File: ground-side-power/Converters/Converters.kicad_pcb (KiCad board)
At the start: 2 copper layers, 30 parts, among them J10 Conn_01x03_Female, J11 Conn_01x03_Female, J12 Conn_01x04_Female, J13 DAQ Voltage Sensing, J14 DAQ Current Sensing, J26 Conn_01x02_Female, U3 K7805-3AR3, U4 INA180, U5 INA180, U6 URB2424LD-20WR3

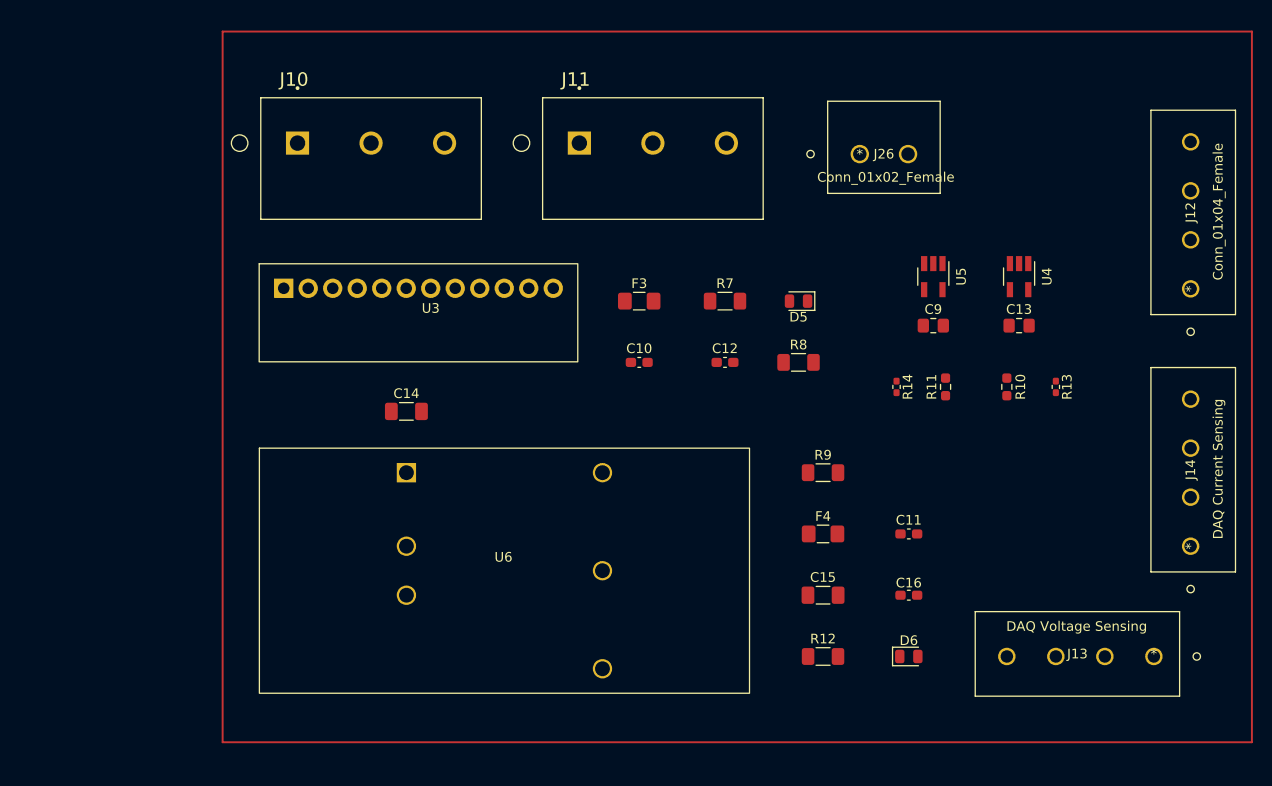
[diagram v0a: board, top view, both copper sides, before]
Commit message: Added Fan Headers + Thermistor
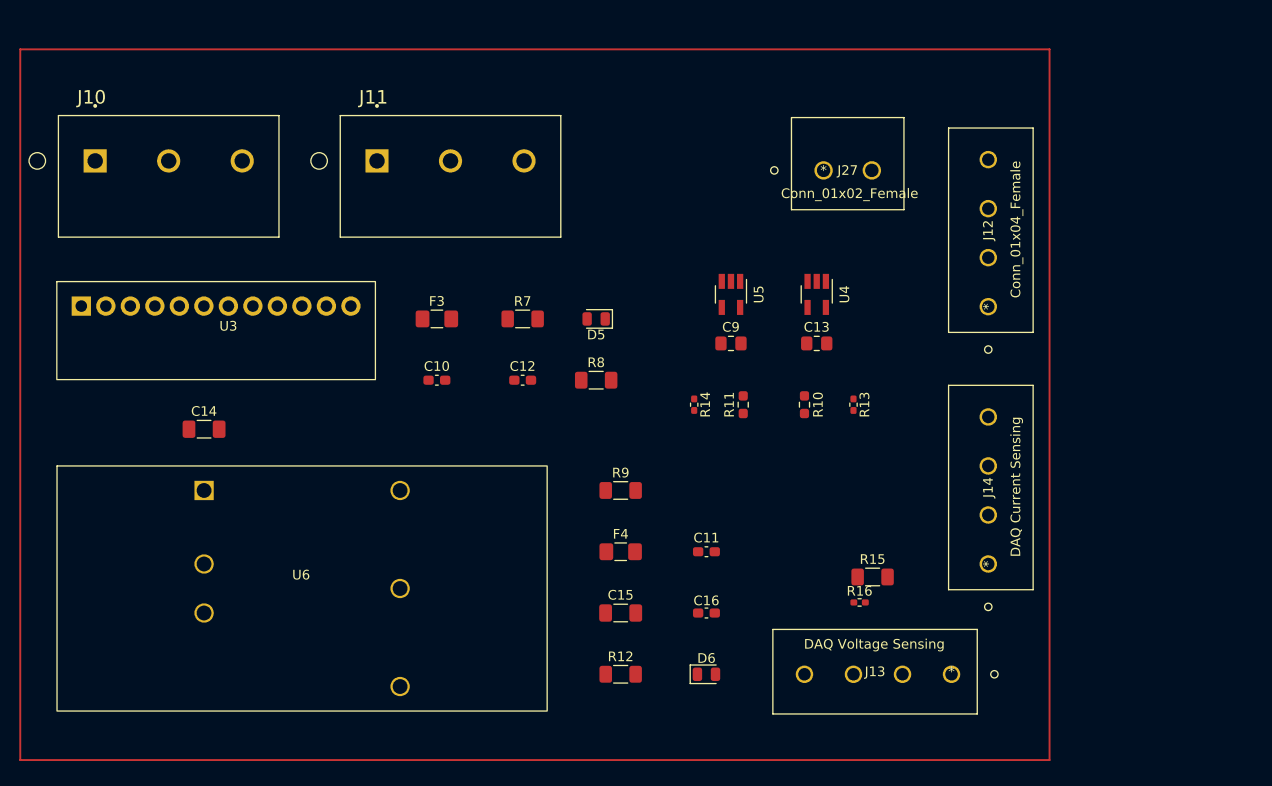
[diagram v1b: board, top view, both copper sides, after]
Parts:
- removed J26: Conn_01x02_Female, GSP:OSTTA020161
- added J27: Conn_01x02_Female, GSP:OSTTA020161, F.Cu at (158.8, 80.4)
- added R15: B57621C5103K062, Resistor_SMD:R_1206_3216Metric_Pad1.30x1.75mm_HandSolder, F.Cu at (163.9, 122.6)
- added R16: 10K, Resistor_SMD:R_0402_1005Metric_Pad0.72x0.64mm_HandSolder, F.Cu at (162.5, 125.2)
- moved C12 21.1 mm to (127.6, 102.2)
- moved C15 21.1 mm to (137.8, 126.3)
- moved C9 21.1 mm to (149.2, 98.4)
- moved D5 21.1 mm to (135.2, 95.8)
- moved F4 21.1 mm to (137.8, 120.0)
- moved J12 21.1 mm to (175.9, 94.6)
- moved J14 21.1 mm to (175.9, 121.2)
- moved R10 21.1 mm to (156.8, 104.7)
- moved R12 21.1 mm to (137.8, 132.7)
- moved R13 21.1 mm to (161.9, 104.7)
- moved R14 21.1 mm to (145.4, 104.7)
- moved R7 21.1 mm to (127.6, 95.8)
- moved R8 21.1 mm to (135.2, 102.2)
- moved R9 21.1 mm to (137.8, 113.6)
- moved U3 21.1 mm to (95.9, 97.1)
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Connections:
- C10 pad 1: (no net) -> Net-(C10-Pad1)
- C10 pad 2: (no net) -> GND
- C11 pad 1: (no net) -> +BATT
- C11 pad 2: (no net) -> GND
- C12 pad 1: (no net) -> +5V
- C12 pad 2: (no net) -> GND
- C13 pad 1: (no net) -> GND
- C13 pad 2: (no net) -> +5V
- C14 pad 1: (no net) -> +BATT
- C14 pad 2: (no net) -> GND
- C15 pad 1: (no net) -> Net-(C15-Pad1)
- C15 pad 2: (no net) -> GND
- C16 pad 1: (no net) -> +24V
- C16 pad 2: (no net) -> GND
- C9 pad 1: (no net) -> GND
- C9 pad 2: (no net) -> +5V
- D5 pad 1: (no net) -> Net-(D5-Pad1)
- D5 pad 2: (no net) -> +5V
- D6 pad 1: (no net) -> Net-(D6-Pad1)
- D6 pad 2: (no net) -> +24V
- F3 pad 1: (no net) -> Net-(C10-Pad1)
- F3 pad 2: (no net) -> /5V_Sense+
- F4 pad 1: (no net) -> Net-(C15-Pad1)
- F4 pad 2: (no net) -> /24V_Sense+
- J10 pad 1: (no net) -> +BATT
- J10 pad 2: (no net) -> /+12V
- J10 pad 3: (no net) -> GND
- J11 pad 1: (no net) -> /12V_OUT
- J11 pad 2: (no net) -> /TOTAL_OUT
- J11 pad 3: (no net) -> /12_VOLTAGE
- J12 pad 1: (no net) -> +5V
- J12 pad 2: (no net) -> /+12V
- J12 pad 3: (no net) -> +24V
- J12 pad 4: (no net) -> GND
- J13 pad 1: (no net) -> /Temp
- J13 pad 2: (no net) -> /5V_VOLTAGE
- J13 pad 3: (no net) -> /12_VOLTAGE
- J13 pad 4: (no net) -> /24V_VOLTAGE
- J14 pad 1: (no net) -> /TOTAL_OUT
- J14 pad 2: (no net) -> /5V_OUT
- J14 pad 3: (no net) -> /12V_OUT
- J14 pad 4: (no net) -> /24V_OUT
- R10 pad 1: (no net) -> +24V
- R10 pad 2: (no net) -> /24V_VOLTAGE
- R11 pad 1: (no net) -> +5V
- R11 pad 2: (no net) -> /5V_VOLTAGE
- R12 pad 1: (no net) -> GND
- R12 pad 2: (no net) -> Net-(D6-Pad1)
- R13 pad 1: (no net) -> /24V_VOLTAGE
- R13 pad 2: (no net) -> GND
- R14 pad 1: (no net) -> /5V_VOLTAGE
- R14 pad 2: (no net) -> GND
- R7 pad 1: (no net) -> /5V_Sense+
- R7 pad 2: (no net) -> +5V
- R8 pad 1: (no net) -> GND
- R8 pad 2: (no net) -> Net-(D5-Pad1)
- R9 pad 1: (no net) -> +24V
- R9 pad 2: (no net) -> /24V_Sense+
- U3 pad 1: (no net) -> unconnected-(U3-Pad1)
- U3 pad 10: (no net) -> Net-(C10-Pad1)
- U3 pad 11: (no net) -> Net-(C10-Pad1)
- U3 pad 12: (no net) -> unconnected-(U3-Pad12)
- U3 pad 2: (no net) -> +BATT
- U3 pad 3: (no net) -> +BATT
- U3 pad 4: (no net) -> +BATT
- U3 pad 5: (no net) -> GND
- U3 pad 6: (no net) -> GND
- U3 pad 7: (no net) -> GND
- U3 pad 8: (no net) -> GND
- U3 pad 9: (no net) -> Net-(C10-Pad1)
- U4 pad 1: (no net) -> /5V_OUT
- U4 pad 2: (no net) -> GND
- U4 pad 3: (no net) -> /5V_Sense+
- U4 pad 4: (no net) -> +5V
- U4 pad 5: (no net) -> +5V
- U5 pad 1: (no net) -> /24V_OUT
- U5 pad 2: (no net) -> GND
- U5 pad 3: (no net) -> /24V_Sense+
- U5 pad 4: (no net) -> +24V
- U5 pad 5: (no net) -> +5V
- U6 pad 1: (no net) -> unconnected-(U6-Pad1)
- U6 pad 2: (no net) -> GND
- U6 pad 3: (no net) -> +BATT
- U6 pad 4: (no net) -> Net-(C15-Pad1)
- U6 pad 5: (no net) -> GND
- U6 pad 6: (no net) -> unconnected-(U6-Pad6)

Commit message: PCB Layout First Draft
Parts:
- added ?: , clipboard:6b5716c7-8553-4764-af17-05841c85de2e, F.Cu at (152.4, 68.7)
- added ?: , clipboard:6b5716c7-8553-4764-af17-05841c85de2e, F.Cu at (152.1, 132.5)
- added ?: , clipboard:6b5716c7-8553-4764-af17-05841c85de2e, F.Cu at (81.2, 132.0)
- added ?: , clipboard:6b5716c7-8553-4764-af17-05841c85de2e, F.Cu at (81.3, 69.3)
- C11, C13, C14, C15, C9, F3, F4, R10, R11, R13, R14, R15, R16, R7, R9, U4, U5: moved to B.Cu
- moved J13 75.4 mm to (96.7, 134.2), turned to 0 degrees
- moved R16 69.9 mm to (92.7, 129.0), turned to 180 degrees
- moved R15 66.7 mm to (97.5, 129.0), turned to 180 degrees
- moved J14 59.1 mm to (118.3, 134.2), turned to 0 degrees
- moved R13 56.2 mm to (111.3, 129.0), turned to 180 degrees
- moved R11 49.9 mm to (106.9, 129.0), turned to 180 degrees
- moved R14 49.2 mm to (102.6, 129.0), turned to 180 degrees
- moved C11 48.9 mm to (105.4, 93.7), turned to 90 degrees
- moved R10 48.1 mm to (115.3, 129.0), turned to 180 degrees
- moved J10 46.2 mm to (129.5, 79.2), turned to 180 degrees
- moved U5 42.1 mm to (125.7, 128.3), turned to 0 degrees
- moved C13 41.1 mm to (131.1, 129.3), turned to 180 degrees
- moved U4 30.7 mm to (127.5, 90.9)
- moved J12 27.7 mm to (149.1, 101.4)
- moved R8 27.4 mm to (149.9, 79.0)
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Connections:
- J11 pad 1: /12V_OUT -> /12_VOLTAGE
- J11 pad 3: /12_VOLTAGE -> /12V_OUT
- J12 pad 1: +5V -> +24V
- J12 pad 2: /+12V -> GND
- J12 pad 3: +24V -> /+12V
- J12 pad 4: GND -> +5V
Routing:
- net +5V: track 0.00 -> 137.9 mm, vias 0 -> 3
- net /12V_OUT: track 0.00 -> 105.7 mm
- net /TOTAL_OUT: track 0.00 -> 96.9 mm
- net /12_VOLTAGE: track 0.00 -> 87.9 mm
- net +24V: track 0.00 -> 78.0 mm
- net /5V_OUT: track 0.00 -> 71.3 mm, vias 0 -> 2
- net /+12V: track 0.00 -> 32.1 mm
- net GND: track 0.00 -> 27.7 mm, vias 0 -> 6
- net Net-(C10-Pad1): track 0.00 -> 15.8 mm
- net /Temp: track 0.00 -> 12.1 mm
- net /24V_OUT: track 0.00 -> 11.5 mm
- net /24V_VOLTAGE: track 0.00 -> 11.4 mm
- net Net-(C15-Pad1): track 0.00 -> 10.9 mm
- net /5V_VOLTAGE: track 0.00 -> 10.6 mm
- net /24V_Sense+: track 0.00 -> 10.2 mm
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- added copper zone on B.Cu, net +BATT
- added copper zone on F.Cu, net GND
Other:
- board outline added: 81.8 x 73.7 mm
- board text added: "+12"
- board text added: "+12 Current"
- board text added: "+12 Voltage"
- board text added: "+24"
- board text added: "+5"
- board text added: "+BATT"
- board text added: "0"
- board text added: "Current"
- board text added: "Temp"
- board text added: "Total"
- board text added: "Total Current"
- board text added: "Voltage"

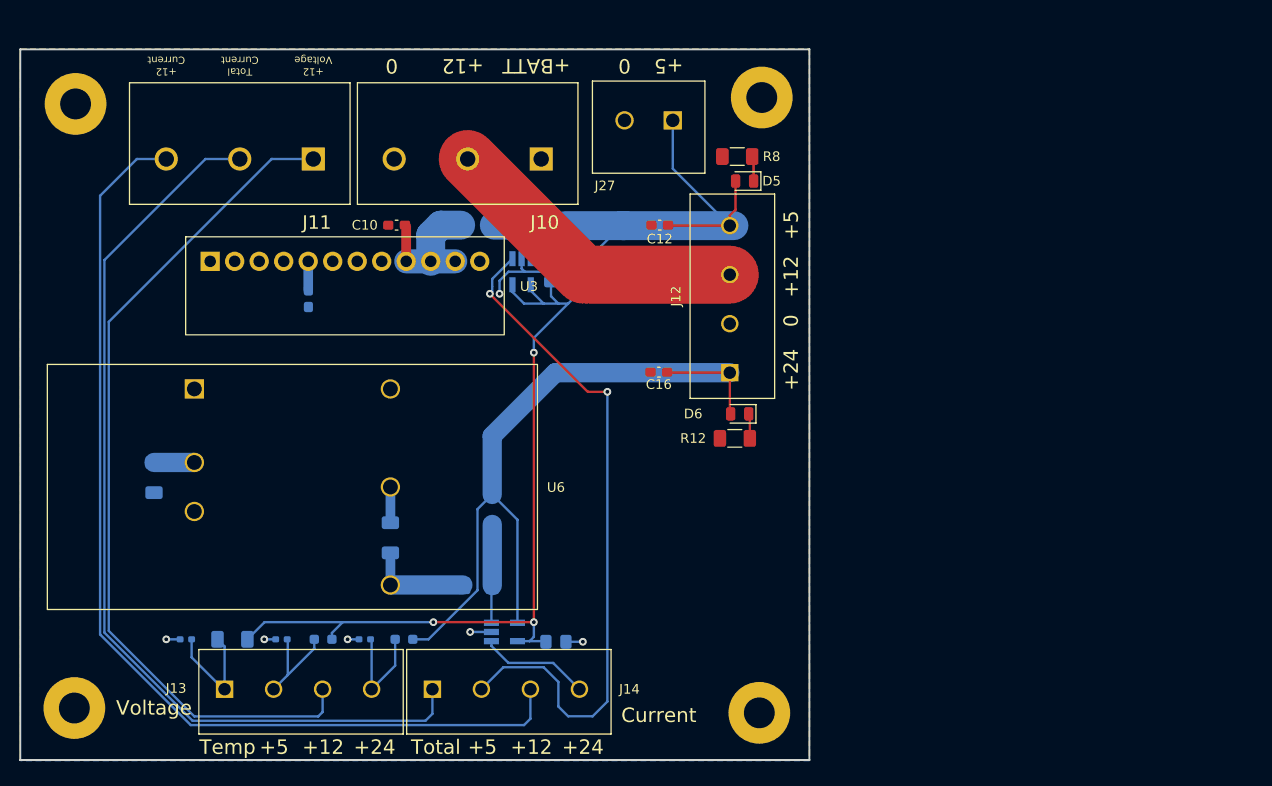
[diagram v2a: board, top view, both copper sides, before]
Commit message: Address Input and Converter Comments
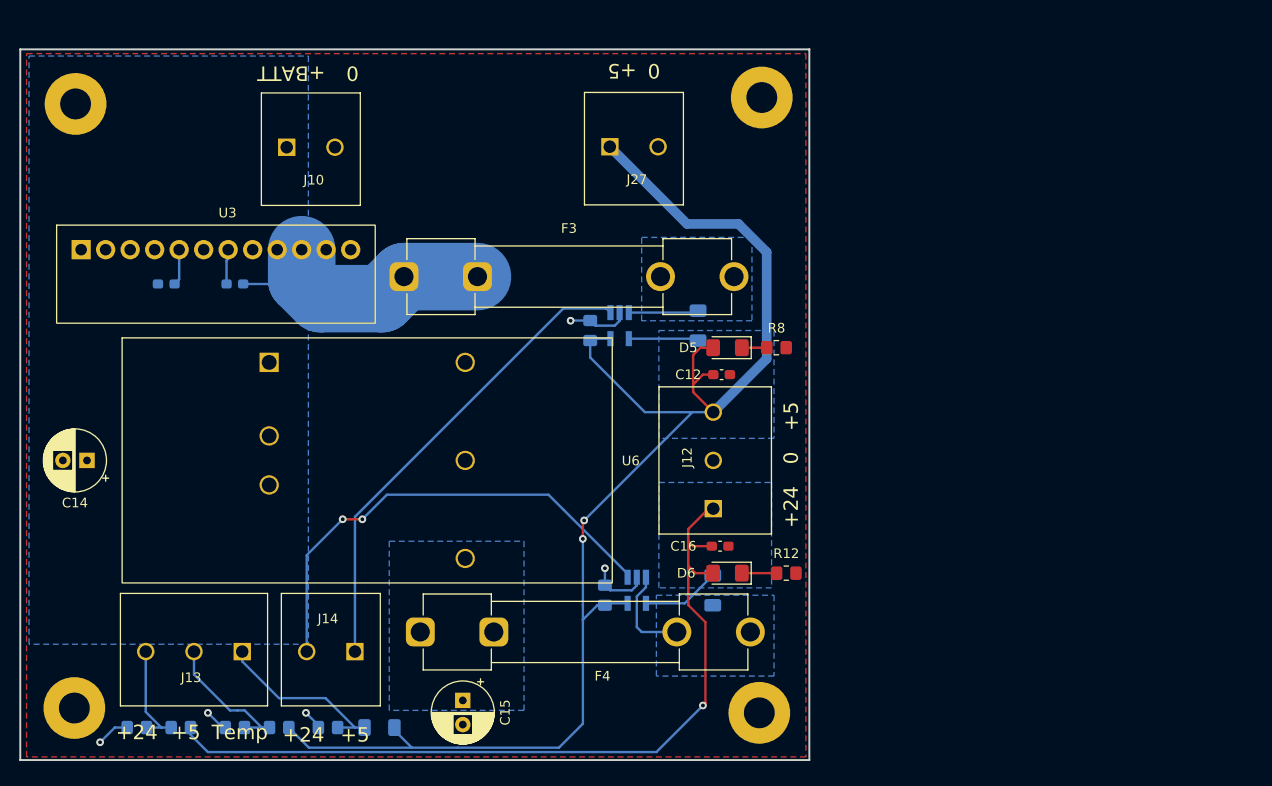
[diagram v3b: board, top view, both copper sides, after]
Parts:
- removed J11: Conn_01x03_Female, GSP:TB005-762-03BE
- C10: moved to B.Cu
- C14, C15: footprint Capacitor_SMD:C_1206_3216Metric_Pad1.33x1.80mm_HandSolder -> Capacitor_THT:CP_Radial_D6.3mm_P2.50mm; moved to F.Cu
- D5, D6: footprint Diode_SMD:D_0805_2012Metric -> Diode_SMD:D_1206_3216Metric_Pad1.42x1.75mm_HandSolder
- F3, F4: footprint Fuse:Fuse_1206_3216Metric_Pad1.42x1.75mm_HandSolder -> Fuse:Fuseholder_Clip-6.3x32mm_Littelfuse_102_122_Inline_P34.21x7.62mm_D1.98mm_Horizontal; moved to F.Cu
- J10: footprint GSP:TB005-762-03BE -> GSP:1935310
- J12, J13: footprint GSP:EB21A-04-D -> GSP:1935323
- J14: footprint GSP:EB21A-04-D -> GSP:1935310
- J27: footprint GSP:OSTTA020161 -> GSP:1935310
- R10, R11: footprint Resistor_SMD:R_0603_1608Metric_Pad0.98x0.95mm_HandSolder -> Resistor_SMD:R_0805_2012Metric_Pad1.20x1.40mm_HandSolder
- R12, R8: footprint Resistor_SMD:R_1206_3216Metric_Pad1.30x1.75mm_HandSolder -> Resistor_SMD:R_0805_2012Metric_Pad1.20x1.40mm_HandSolder
- R13, R14, R16: footprint Resistor_SMD:R_0402_1005Metric_Pad0.72x0.64mm_HandSolder -> Resistor_SMD:R_0805_2012Metric_Pad1.20x1.40mm_HandSolder
- moved J10 26.4 mm to (103.2, 78.0), turned to 0 degrees
- moved R13 25.3 mm to (87.6, 138.2)
- moved R10 24.9 mm to (92.2, 138.2)
- moved R9 24.3 mm to (147.3, 124.0)
- moved R8 20.2 mm to (153.9, 98.8), turned to 180 degrees
- moved C16 19.1 mm to (148.1, 119.4), turned to 0 degrees
- moved R7 18.9 mm to (145.8, 96.5), turned to -90 degrees
- moved C15 18.5 mm to (121.4, 135.4), turned to -90 degrees
- moved C10 17.8 mm to (97.8, 92.2)
- moved R15 17.8 mm to (112.8, 138.2)
- moved D5 17.4 mm to (148.8, 98.8)
- moved R16 17.3 mm to (107.4, 138.2)
- moved C12 16.8 mm to (148.2, 101.6), turned to 0 degrees
- moved D6 16.6 mm to (148.8, 122.2)
- moved R12 15.0 mm to (154.9, 122.2), turned to 180 degrees
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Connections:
- J10 pad 2: /+12V -> GND
- J12 pad 3: /+12V -> +5V
- J13 pad 3: /12_VOLTAGE -> /24V_VOLTAGE
- J14 pad 1: /TOTAL_OUT -> /5V_OUT
- J14 pad 2: /5V_OUT -> /24V_OUT
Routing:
- net /12V_OUT: track 105.7 -> 0.00 mm
- net /TOTAL_OUT: track 96.9 -> 0.00 mm
- net /12_VOLTAGE: track 87.9 -> 0.00 mm
- net /24V_OUT: track 11.5 -> 49.6 mm, vias 0 -> 2
- net /+12V: track 32.1 -> 0.00 mm
- net /5V_OUT: track 71.3 -> 49.6 mm, vias 2 -> 0
- net +5V: track 137.9 -> 155.2 mm, vias 3 -> 2
- net +24V: track 78.0 -> 92.9 mm, vias 0 -> 1
- net Net-(C10-Pad1): track 15.8 -> 29.3 mm
- net Net-(C15-Pad1): track 10.9 -> 0.00 mm
- net /Temp: track 12.1 -> 18.3 mm
- net /5V_VOLTAGE: track 10.6 -> 14.3 mm
- net Net-(D6-Pad1): track 2.58 -> 3.61 mm
- net GND: track 27.7 -> 28.0 mm, vias 6 -> 5
- added copper zone on B.Cu, net +24V
- added copper zone on B.Cu, net +5V
- added copper zone on B.Cu, net /24V_Sense+
- added copper zone on B.Cu, net /5V_Sense+
- added copper zone on B.Cu, net Net-(C15-Pad1)
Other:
- board text removed: "+12"
- board text removed: "+12 Current"
- board text removed: "+12 Voltage"
- board text removed: "Current"
- board text removed: "Total"
- board text removed: "Total Current"
- board text removed: "Voltage"

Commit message: Resolved Final Issues
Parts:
- added G***: LOGO, rlcs:rocketry_logo_small, F.Cu at (143.5, 75.5)
- C10, C11, C12, C16: footprint Capacitor_SMD:C_0603_1608Metric_Pad1.08x0.95mm_HandSolder -> Capacitor_SMD:C_0805_2012Metric_Pad1.18x1.45mm_HandSolder
- R7, R9: footprint Resistor_SMD:R_1206_3216Metric_Pad1.30x1.75mm_HandSolder -> Resistor_SMD:R_2512_6332Metric_Pad1.40x3.35mm_HandSolder
- moved ? 29.0 mm to (181.1, 131.4)
- moved ? 28.8 mm to (181.1, 66.9)
- moved C16 28.3 mm to (176.4, 118.6)
- moved C12 28.3 mm to (176.5, 100.5)
- moved J27 28.2 mm to (164.8, 76.5)
- moved D6 28.2 mm to (177.0, 121.2)
- moved D5 28.2 mm to (177.0, 97.8)
- moved R7 28.2 mm to (174.0, 95.5)
- moved R9 28.2 mm to (175.5, 122.9)
- moved C11 28.2 mm to (118.9, 91.2)
- moved C14 28.2 mm to (110.7, 109.5)
- moved J14 28.2 mm to (138.4, 129.3)
- moved R11 28.2 mm to (130.6, 137.2)
- moved R13 28.2 mm to (115.8, 137.2)
- moved R15 28.2 mm to (141.0, 137.2)
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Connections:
- J10 pad 1: +BATT -> GND
- J10 pad 2: GND -> +BATT
- J27 pad 1: +5V -> GND
- J27 pad 2: GND -> +5V
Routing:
- net +5V: track 155.2 -> 152.5 mm
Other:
- board size 81.8 x 73.7 mm -> 82.8 x 74.4 mm
- board text added: "Ground Side Power Converter Board Domenic Hampson Elias Kountouris"
